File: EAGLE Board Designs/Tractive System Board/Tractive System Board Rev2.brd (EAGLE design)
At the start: 206.7 x 150.3 mm, 183 parts, among them J3 CONNECTOR-8__, J5 CONNECTOR-4__, K4 RELAY_SPST_NC_POLARIZED_3550_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, K5 RELAY_SPST_NO_3550_12, Q2 TRANSISTOR_N_MOS__PMV15ENEA, U1 LTC6994_1, U10 DCM4623TD2J13D0T70, U11 RELAY_SOLIDSTATE_NC_AG, U15 LOGICGATE_INVERTER_DCKR, U16 LTC3639, U17 VOLTAGE_REGULATOR_ADJ_LR8_DPAK, U18 ISO224B_AIRGAP, U19 ISO224B_AIRGAP, U2 VOLTAGE_REGULATOR_SOT223_5V

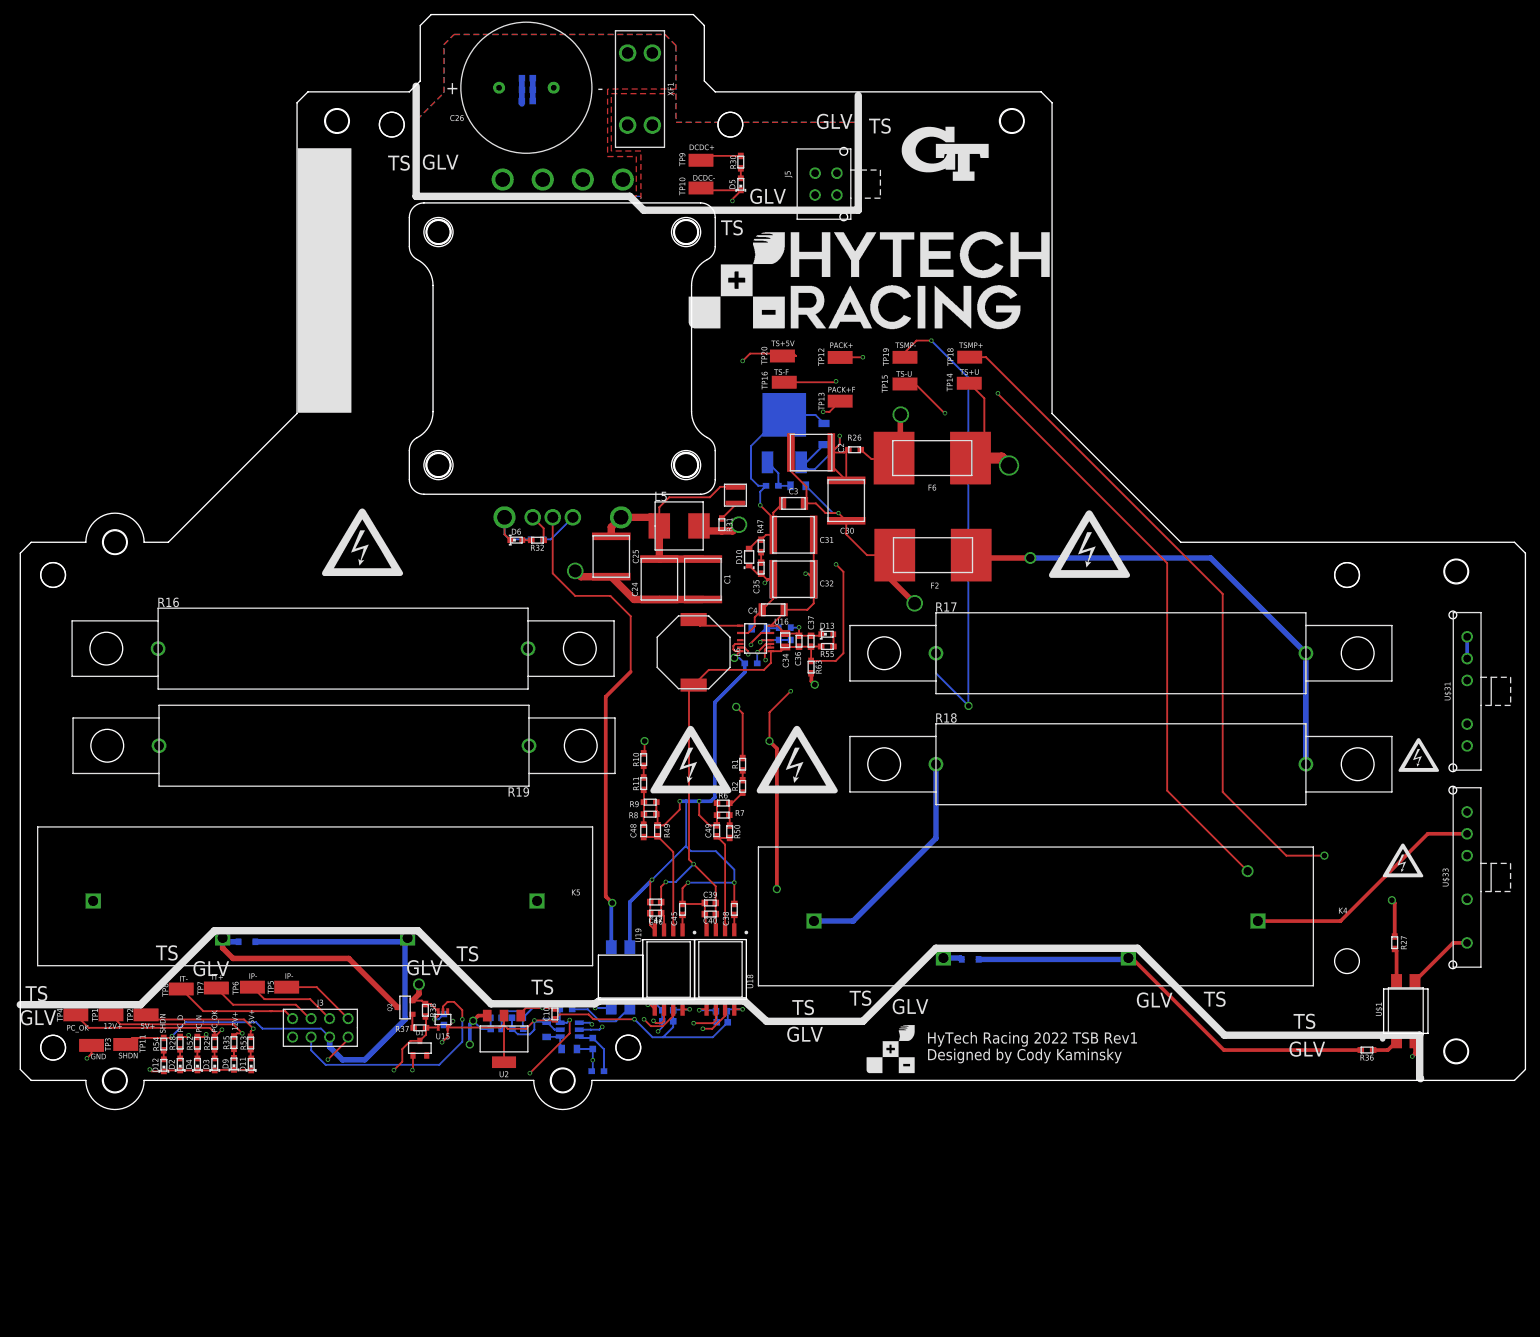
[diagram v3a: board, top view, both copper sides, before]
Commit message: fixed drc errors
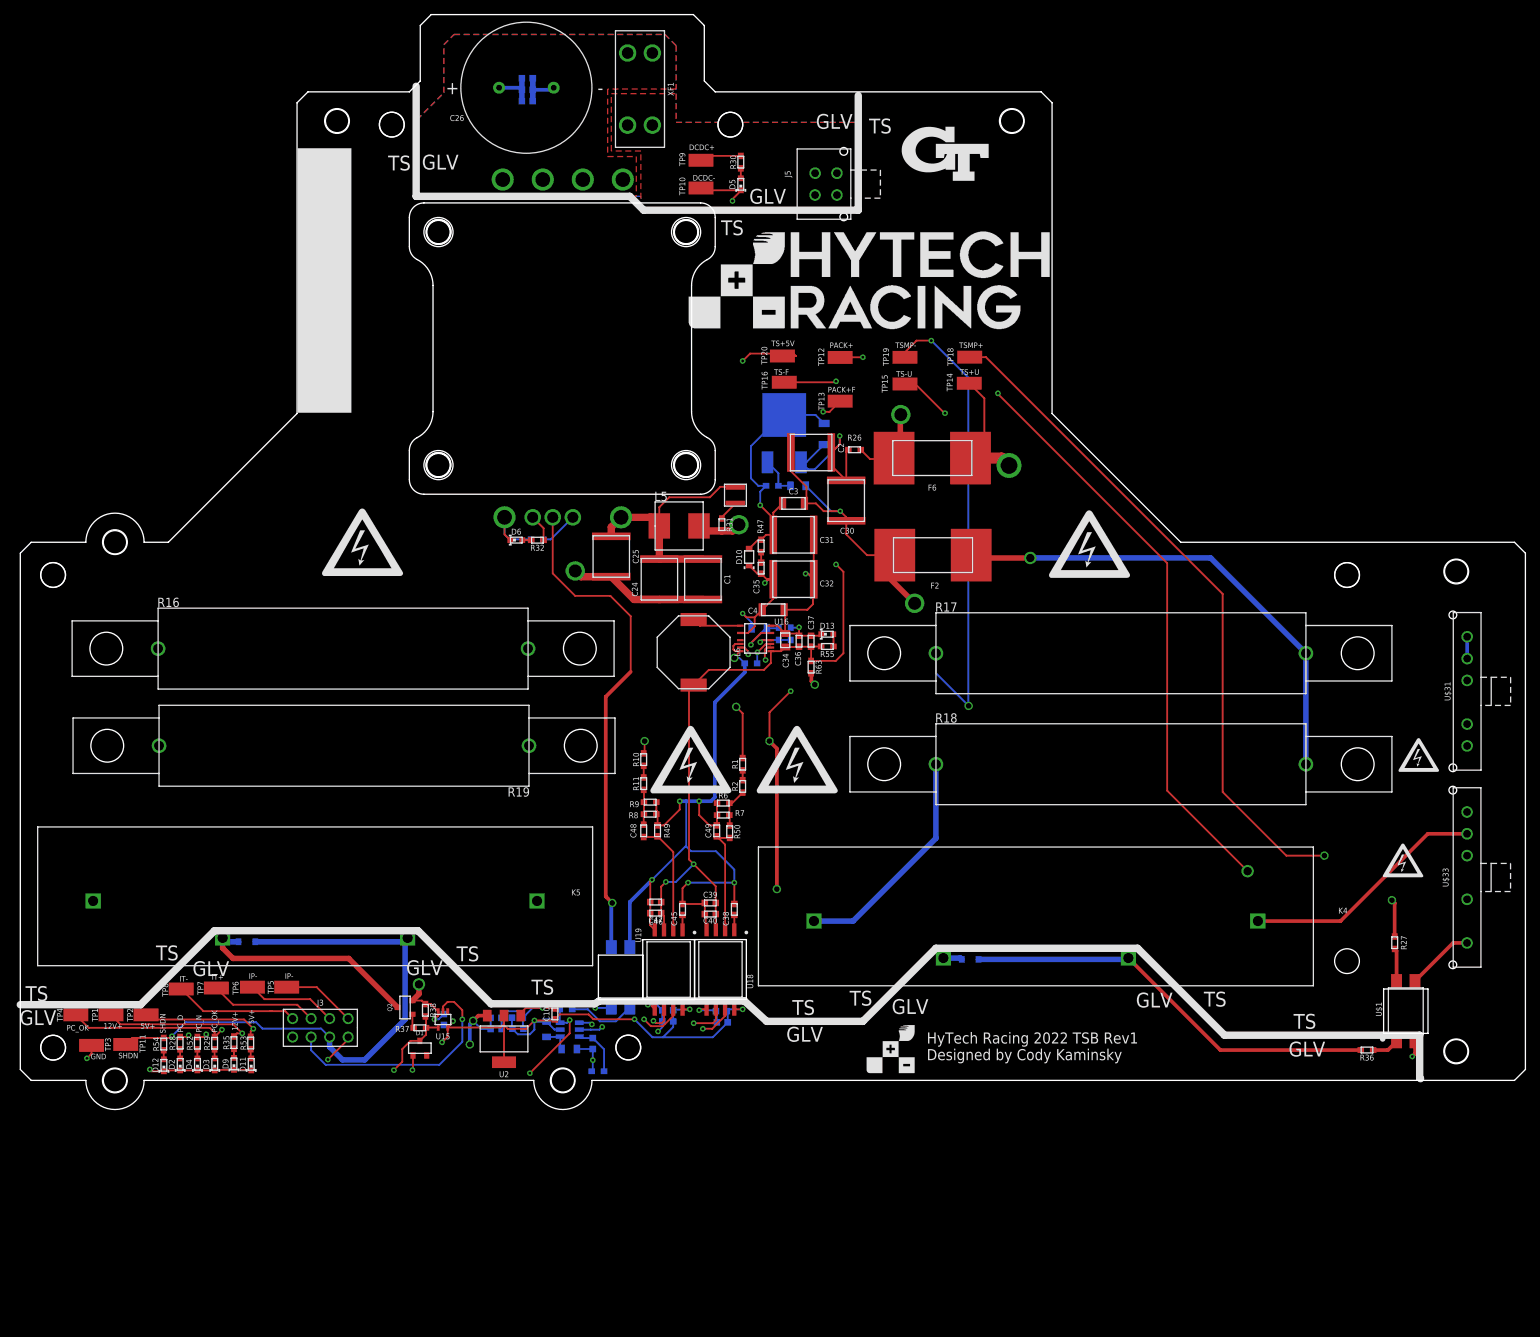
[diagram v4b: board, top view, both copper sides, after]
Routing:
- net N$61: track 17.5 -> 21.2 mm, vias 1 -> 2
- net DCDC-: track 10.8 -> 13.7 mm
- net N$46: track 3.55 -> 6.40 mm
- net N$15: track 26.9 -> 24.2 mm
- net N$58: track 36.2 -> 33.7 mm
- net TS-FUSED: track 413.6 -> 414.5 mm
- net IT+: track 76.4 -> 75.8 mm

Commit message: Minor fixes
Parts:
- added U$76: (no value), HyTechManufacturing:LOGO_GT_LARGE
- added U$77: (no value), HyTechManufacturing:LOGO_HYTECH_EXTRA_LARGE
- moved C32 0.13 mm to (106.2, 67.4)
- moved C33 0.13 mm to (106.2, 67.4)
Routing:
- net N$61: track 21.2 -> 27.2 mm, vias 2 -> 1
- net TS-FUSED: track 414.5 -> 416.9 mm
- net ENABLE: track 68.1 -> 68.6 mm
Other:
- outline, holes or cut-outs redrawn
